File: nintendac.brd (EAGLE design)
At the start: 43 x 43 mm, 35 parts, among them IC2 REG1117, U1 STM32F10XRXT6, X1 USB-MICROB

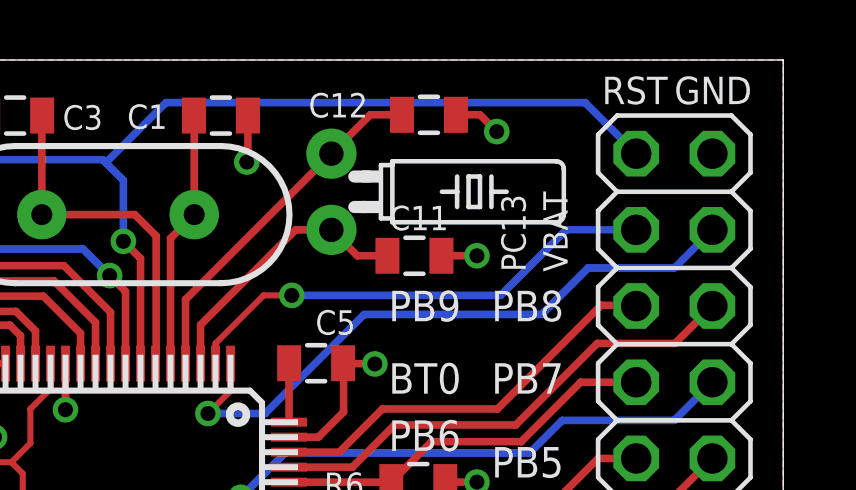
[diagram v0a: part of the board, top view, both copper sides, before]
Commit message: silkscreen cleanup
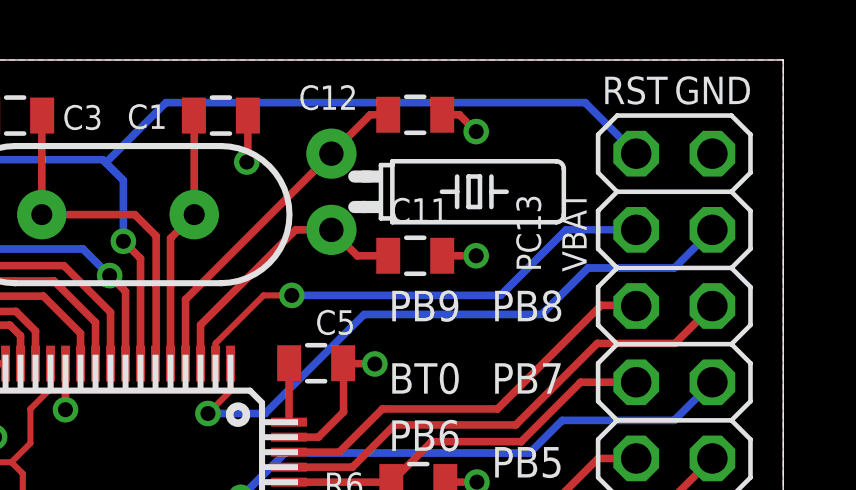
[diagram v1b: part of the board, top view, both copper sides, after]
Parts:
- moved C12 0.46 mm to (30.7, 41.2)
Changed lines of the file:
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@@
 <text x="33.274" y="34.29" size="1.016" layer="25">PB8</text>
 <text x="29.845" y="34.29" size="1.016" layer="25">PB9</text>
-<text x="35.814" y="35.941" size="0.8128" layer="25" rot="R90">VBAT</text>
-<text x="34.417" y="35.941" size="0.8128" layer="25" rot="R90">PC13</text>
+<text x="36.449" y="35.941" size="0.8128" layer="25" rot="R90">VBAT</text>
+<text x="34.925" y="35.941" size="0.8128" layer="25" rot="R90">PC13</text>
 <text x="36.957" y="41.529" size="0.9144" layer="25">RST</text>
 <text x="6.858" y="21.844" size="1.016" layer="25">PB0</text>
@@
 <attribute name="VALUE" x="29.972" y="35.941" size="1.27" layer="27" ratio="10"/>
 </element>
-<element name="C11" library="backplane" package="0805" value="" x="30.7086" y="36.4744" smashed="yes">
-<attribute name="NAME" x="29.8704" y="37.3253" size="0.8128" layer="25"/>
-<attribute name="VALUE" x="29.6926" y="35.0774" size="0.4064" layer="27"/>
-</element>
-<element name="C12" library="backplane" package="0805" value="" x="31.1912" y="41.1734" smashed="yes">
-<attribute name="NAME" x="27.178" y="41.0845" size="0.8128" layer="25"/>
-<attribute name="VALUE" x="30.1752" y="39.7764" size="0.4064" layer="27"/>
+<element name="C11" library="backplane" package="0805" value="" x="30.734" y="36.4744" smashed="yes">
+<attribute name="NAME" x="29.8958" y="37.5793" size="0.8128" layer="25"/>
+<attribute name="VALUE" x="29.718" y="35.0774" size="0.4064" layer="27"/>
+</element>
+<element name="C12" library="backplane" package="0805" value="" x="30.734" y="41.1734" smashed="yes">
+<attribute name="NAME" x="26.8478" y="41.3385" size="0.8128" layer="25"/>
+<attribute name="VALUE" x="29.718" y="39.7764" size="0.4064" layer="27"/>
 </element>
 <element name="R8" library="SparkFun-Passives" package="0805" value="" x="12.8778" y="37.4396" smashed="yes" rot="R180">
@@
 <wire x1="28.3464" y1="32.8786" x2="29.3768" y2="32.8786" width="0.254" layer="1"/>
 <wire x1="29.3768" y1="32.8786" x2="29.3878" y2="32.8676" width="0.254" layer="1"/>
-<via x="32.7914" y="36.4744" extent="1-16" drill="0.5"/>
-<via x="33.4518" y="40.6146" extent="1-16" drill="0.5"/>
-<wire x1="32.7914" y1="36.4744" x2="31.6086" y2="36.4744" width="0.254" layer="1"/>
-<wire x1="33.4518" y1="40.6146" x2="32.893" y2="41.1734" width="0.254" layer="1"/>
-<wire x1="32.893" y1="41.1734" x2="32.0912" y2="41.1734" width="0.254" layer="1"/>
+<via x="32.766" y="36.4744" extent="1-16" drill="0.5"/>
+<via x="32.766" y="40.6146" extent="1-16" drill="0.5"/>
 <via x="22.479" y="8.128" extent="1-16" drill="0.508"/>
 <wire x1="22.476" y1="6.096" x2="22.479" y2="6.099" width="0.4064" layer="1"/>
@@
 <wire x1="27.5336" y1="20.6248" x2="26.5828" y2="19.674" width="0.254" layer="1"/>
 <wire x1="26.5828" y1="19.674" x2="26.289" y2="19.674" width="0.254" layer="1"/>
+<wire x1="32.766" y1="40.6146" x2="32.2072" y2="41.1734" width="0.254" layer="1"/>
+<wire x1="32.2072" y1="41.1734" x2="31.634" y2="41.1734" width="0.254" layer="1"/>
+<wire x1="32.766" y1="36.4744" x2="31.634" y2="36.4744" width="0.254" layer="1"/>
 <wire x1="28.2448" y1="12.319" x2="28.3464" y2="12.4206" width="0" layer="19" extent="1-1"/>
 </signal>
@@
 <wire x1="26.7462" y1="37.338" x2="27.94" y2="37.338" width="0.254" layer="1"/>
 <wire x1="27.94" y1="37.338" x2="28.8036" y2="36.4744" width="0.254" layer="1"/>
-<wire x1="28.8036" y1="36.4744" x2="29.8086" y2="36.4744" width="0.254" layer="1"/>
+<wire x1="28.8036" y1="36.4744" x2="29.834" y2="36.4744" width="0.254" layer="1"/>
 </signal>
 <signal name="N$29">
@@
 <wire x1="23.078" y1="35.016" x2="27.94" y2="39.878" width="0.254" layer="1"/>
 <wire x1="27.94" y1="39.878" x2="29.2354" y2="41.1734" width="0.254" layer="1"/>
-<wire x1="29.2354" y1="41.1734" x2="30.2912" y2="41.1734" width="0.254" layer="1"/>
+<wire x1="29.2354" y1="41.1734" x2="29.834" y2="41.1734" width="0.254" layer="1"/>
 </signal>
 <signal name="LDAC">

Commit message: board cleanup
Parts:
- added S2: SWITCH-MOMENTARY-2TURTLE, Adafruit Feather M0 Adalogger:KMR2
- moved C12 0.99 mm to (30.1, 40.4)
- moved C1 0.90 mm to (23.6, 40.5)
- moved C3 0.90 mm to (16.8, 40.5)
- moved R7 0.81 mm to (38.1, 1.45)
- moved C11 0.81 mm to (30.1, 36.0)
- moved C6 0.81 mm to (25.7, 20.1)
- moved LED2 0.81 mm to (21.7, 16.2)
- moved R9 0.81 mm to (18.1, 16.2)
- moved C2 0.81 mm to (23.2, 9.65)
- moved C7 0.81 mm to (12.8, 21.3)
- moved C8 0.81 mm to (11.2, 29.9)
- moved S1 0.81 mm to (10.4, 39.5)
- moved C4 0.81 mm to (23.2, 5.59)
- moved R1 0.81 mm to (2.16, 10.4)
- moved R2 0.81 mm to (4.95, 10.4)
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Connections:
- net GND: now also S2.1
- net N$30: now also S2.3
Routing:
- net +3V3: track 25.8 -> 53.2 mm
- net N$30: track 22.1 -> 28.8 mm
- net GND: track 46.5 -> 49.1 mm
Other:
- board size 43 x 43 mm -> 42 x 42 mm
- board text added: "dekuNukem"
- board text removed: "dekuNukem 2017"
